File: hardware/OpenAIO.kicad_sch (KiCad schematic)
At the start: 0 parts

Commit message: Root sheet: place the sub-sheets; ESC as the 4in1 top sheet
esc_4in1.kicad_sch is OpenESC-20x20's 4in1-mini top sheet (battery input,
shunt and INA186 current sense, 12V/3V3 regulators, four ESC channel
instances). Its channel sub-sheet keeps its original file name ESC.kicad_sch
so the top sheet is untouched. Root sheet: Power, IMU, OSD, Blackbox, Pads,
RP2354A, ESC, RX placed, no wiring.
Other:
- added sheet Blackbox (fc_blackbox.kicad_sch)
- added sheet ESC (esc_4in1.kicad_sch)
- added sheet IMU (fc_imu.kicad_sch)
- added sheet OSD (fc_osd.kicad_sch)
- added sheet Pads (fc_pads.kicad_sch)
- added sheet Power (fc_power.kicad_sch)
- added sheet RP2354A (fc_rp2350a.kicad_sch)
- added sheet RX (rx_esp32c3_sx1281.kicad_sch)
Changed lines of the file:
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@@
-(kicad_sch
-  (version 20260306)
-  (generator "eeschema")
-  (generator_version "10.0")
-  (paper "A4")
-  (sheet_instances
-    (path "/"
-      (page "1")))
-  (embedded_fonts no))

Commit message: Drop the ESC sheets again; CSA taken into fc_power
esc_4in1 and ESC removed from the root and the tree. fc_power carries
Stan's in-progress edits with the current-sense parts.
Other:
- removed sheet ESC

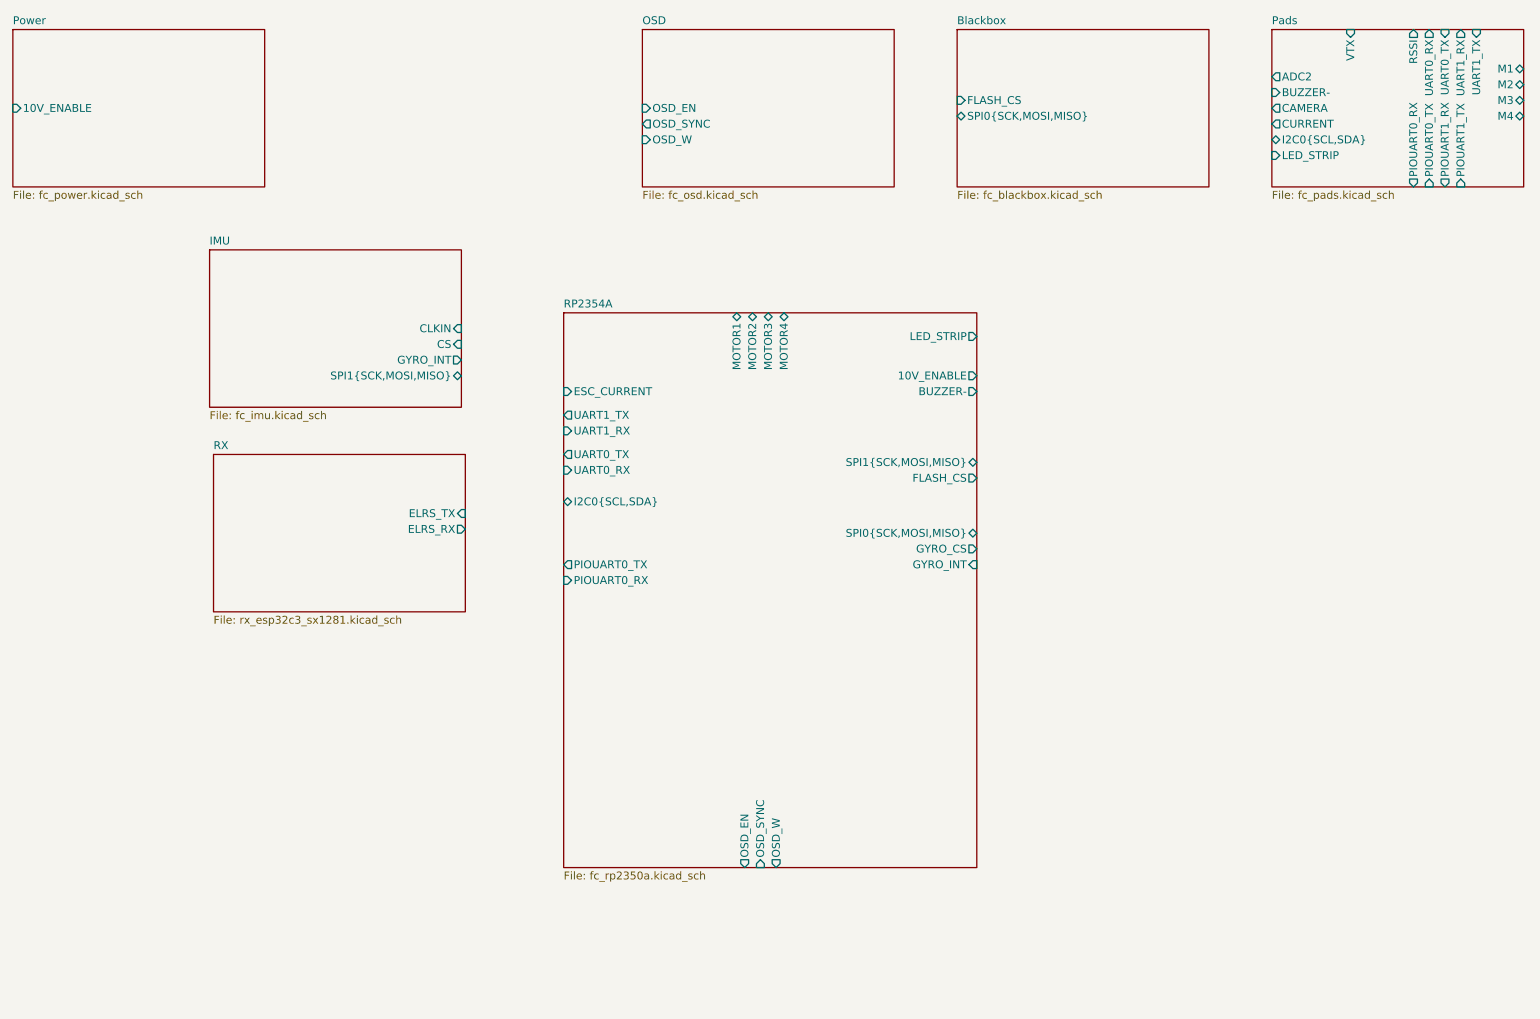
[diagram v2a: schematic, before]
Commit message: Root sheet: ESC1..ESC4 back, one esc_channel instance each
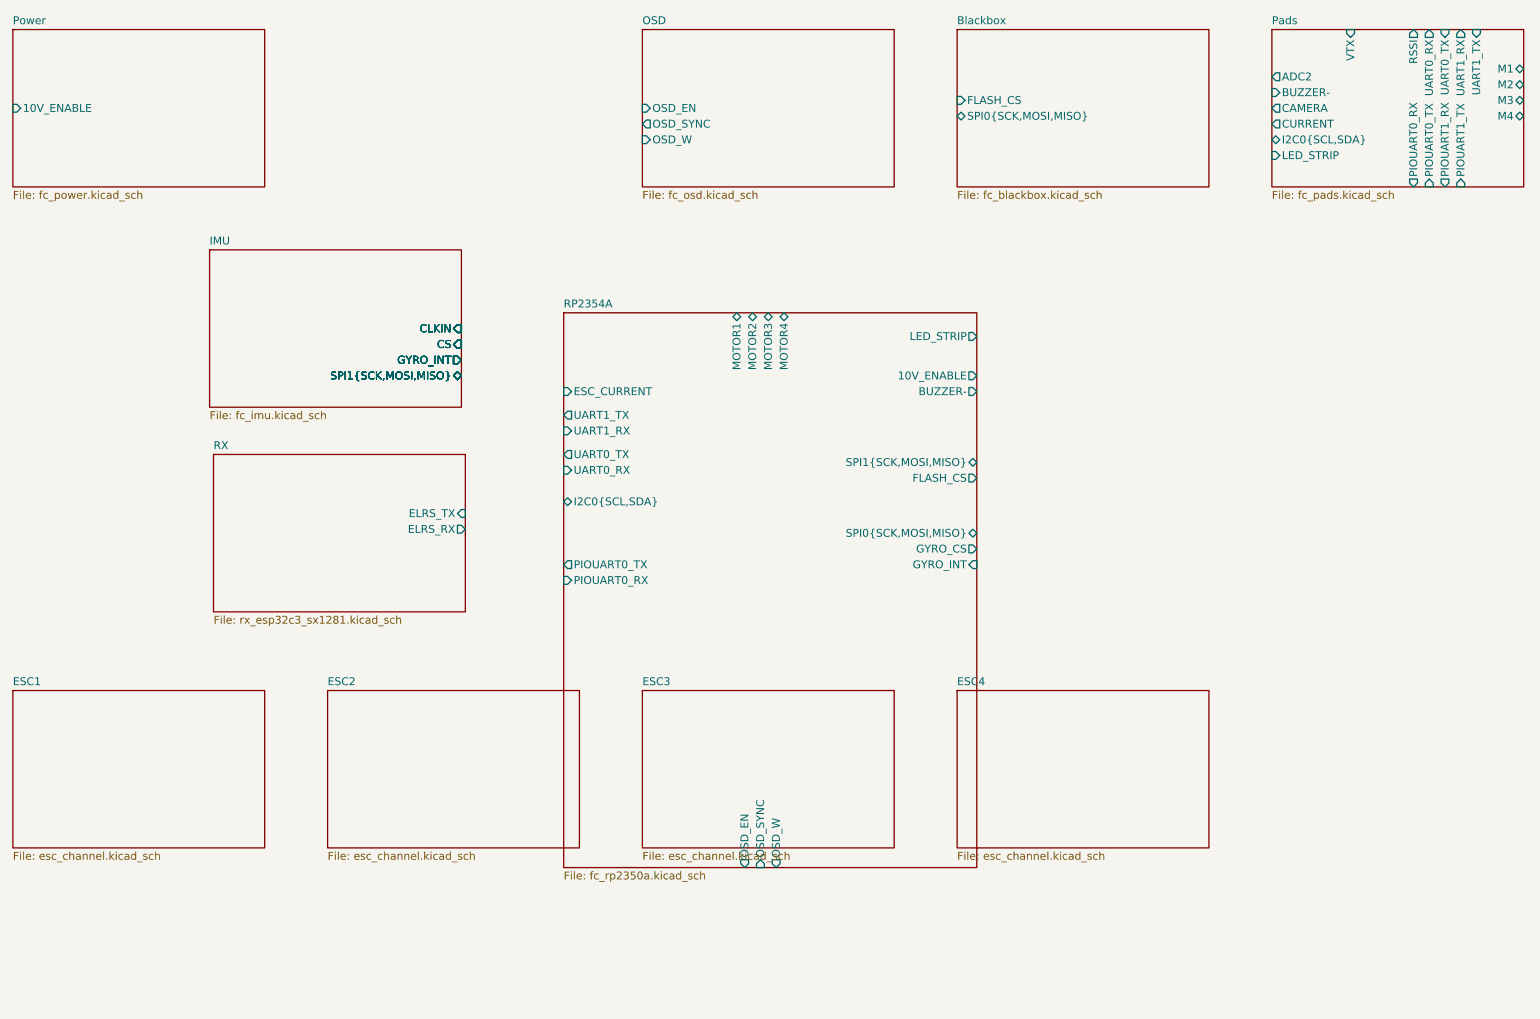
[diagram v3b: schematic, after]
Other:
- added sheet ESC1 (esc_channel.kicad_sch)
- added sheet ESC2 (esc_channel.kicad_sch)
- added sheet ESC3 (esc_channel.kicad_sch)
- added sheet ESC4 (esc_channel.kicad_sch)

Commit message: Restore the root, project and esc_channel to the 21:58 save, before the ESC top sheet
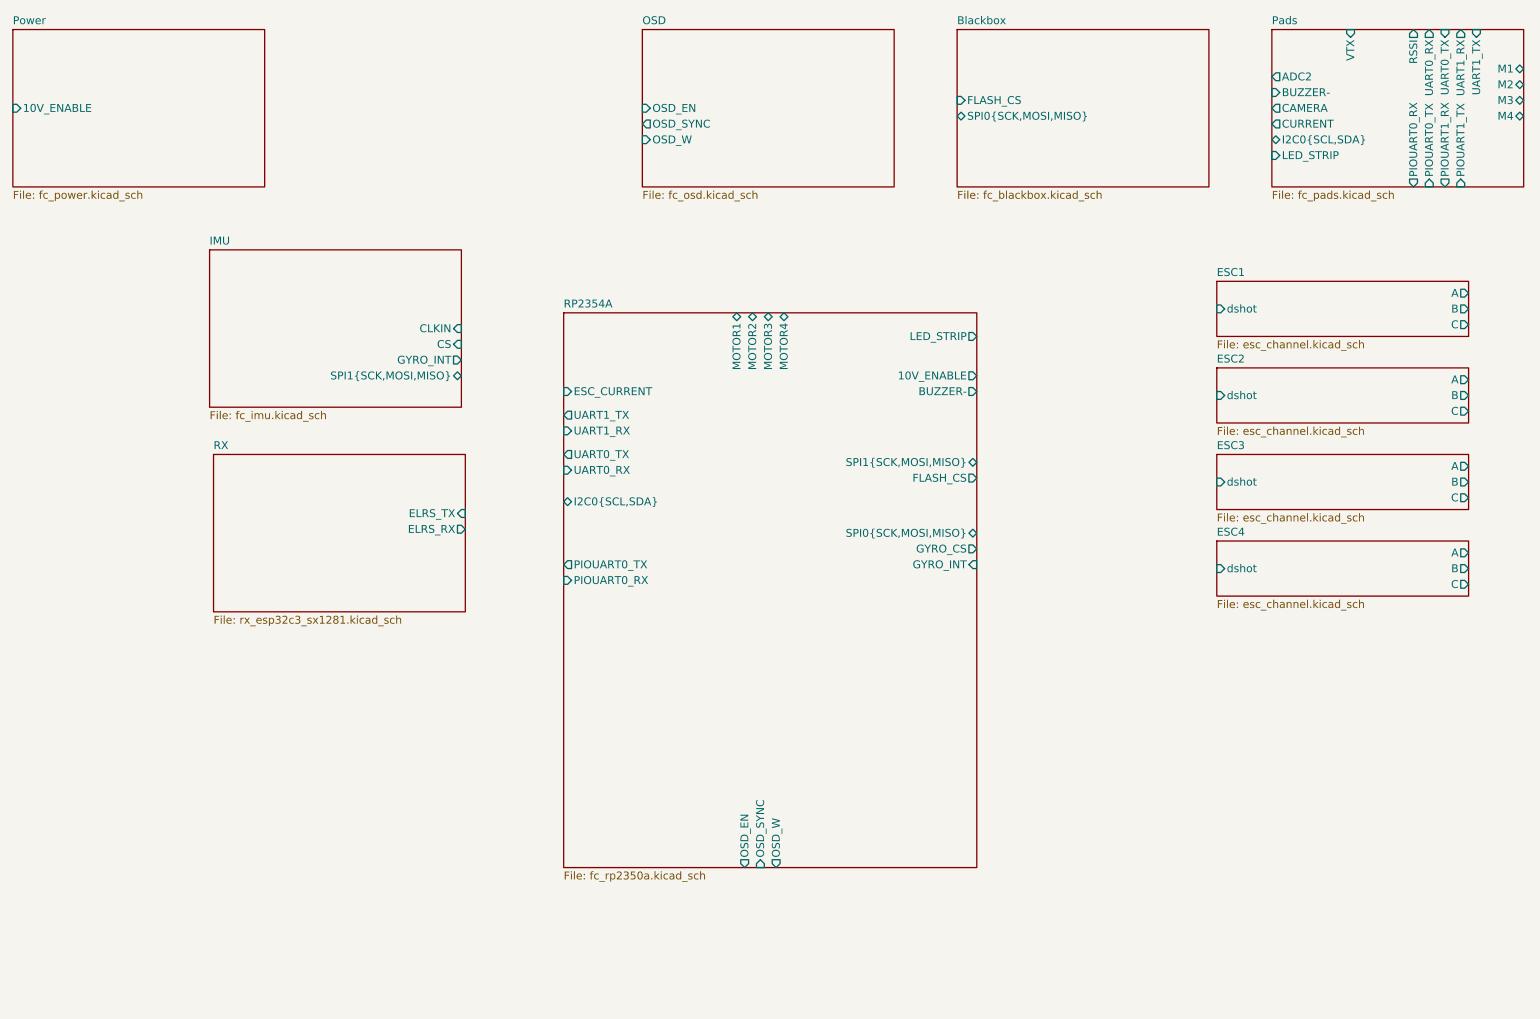
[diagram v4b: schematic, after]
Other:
- sheet ESC1 ports: added A, B, C, dshot; removed CLKIN, CS, GYRO_INT, SPI1{SCK,MOSI,MISO}
- sheet ESC2 ports: added A, B, C, dshot; removed CLKIN, CS, GYRO_INT, SPI1{SCK,MOSI,MISO}
- sheet ESC3 ports: added A, B, C, dshot; removed CLKIN, CS, GYRO_INT, SPI1{SCK,MOSI,MISO}
- sheet ESC4 ports: added A, B, C, dshot; removed CLKIN, CS, GYRO_INT, SPI1{SCK,MOSI,MISO}

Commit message: Net classes: VBAT, Phase, Power, Gate, USB, RF, Analog with colours and patterns
Replaces the stale 50Ohm /ELRS/* patterns inherited from the template.
Widths and clearances start from the line standard (0.09/0.09, via 0.35/0.20)
and the ESC boards' practice; USB and RF geometry still to be checked against
the chosen JLCPCB 6-layer stackup.
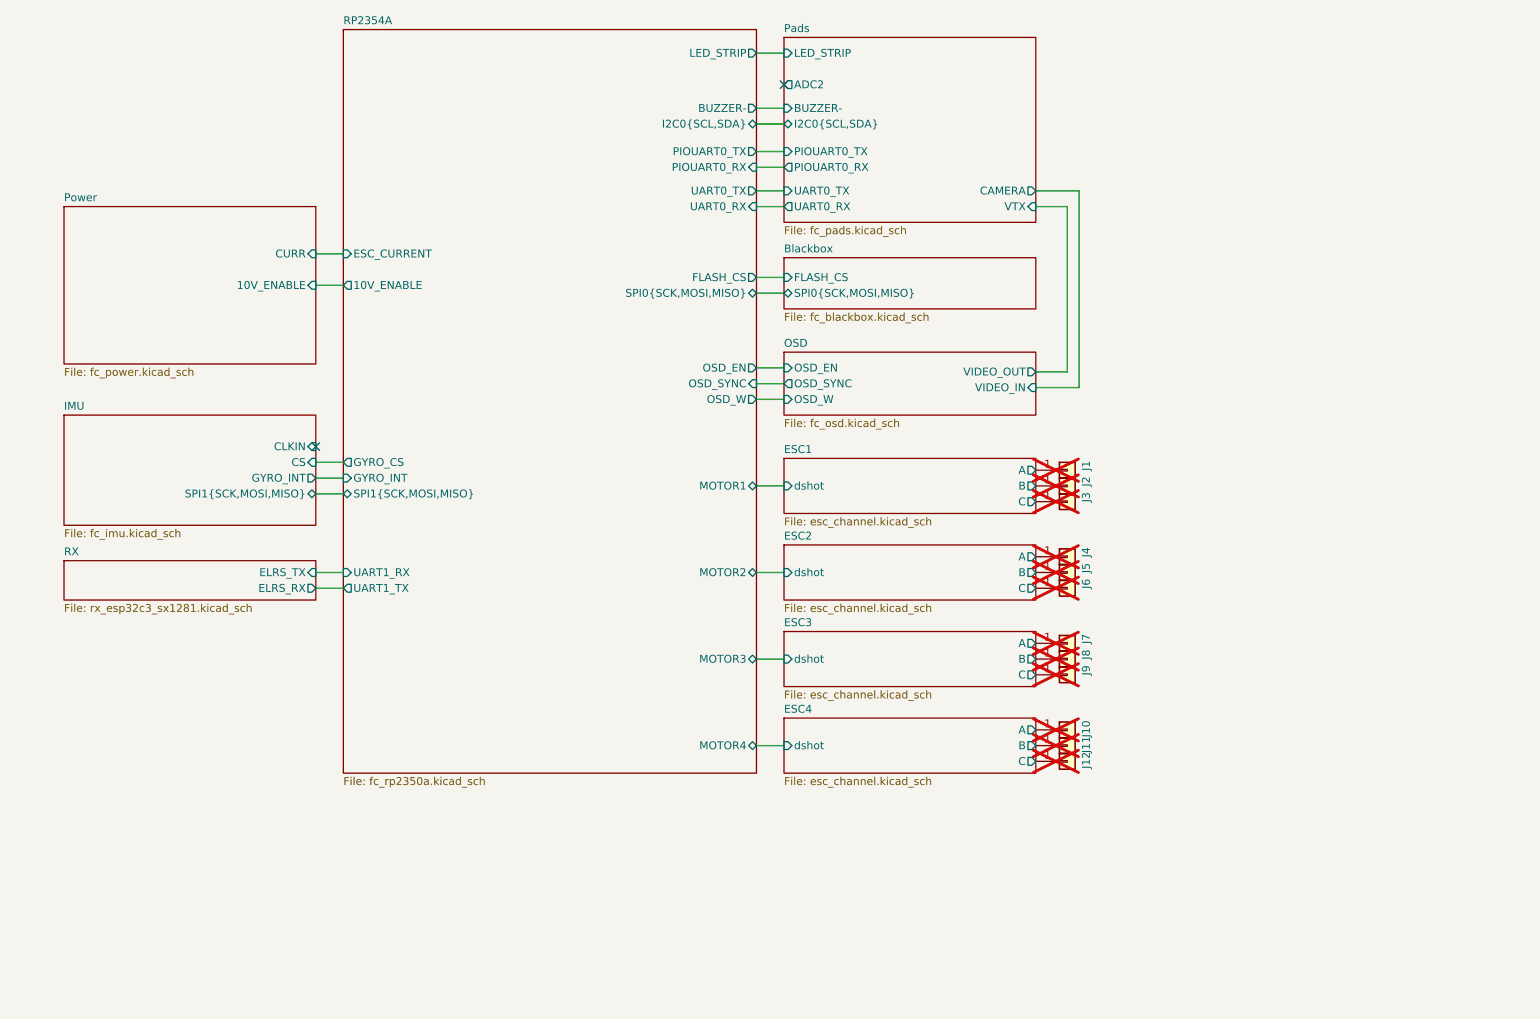
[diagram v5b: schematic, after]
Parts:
- added J1, J10, J11, J12, J2, J3, J4, J5, J6, J7, J8, J9: 5V, lib:small_pad, symbol Connector_Generic:Conn_01x01
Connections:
- net ESC1/A: now also J1.1 (Pin_1)
- net ESC1/B: now also J2.1 (Pin_1)
- net ESC1/C: now also J3.1 (Pin_1)
- net ESC2/A: now also J4.1 (Pin_1)
- net ESC2/B: now also J5.1 (Pin_1)
- net ESC2/C: now also J6.1 (Pin_1)
- net ESC3/A: now also J7.1 (Pin_1)
- net ESC3/B: now also J8.1 (Pin_1)
- net ESC3/C: now also J9.1 (Pin_1)
- net ESC4/A: now also J10.1 (Pin_1)
- net ESC4/B: now also J11.1 (Pin_1)
- net ESC4/C: now also J12.1 (Pin_1)
- no-connect marks 0 -> 2
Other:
- sheet OSD ports: added VIDEO_IN, VIDEO_OUT; removed none
- sheet Pads ports: added none; removed CURRENT, M1, M2, M3, M4, PIOUART1_RX, PIOUART1_TX, RSSI, UART1_RX, UART1_TX
- sheet Power ports: added CURR; removed none

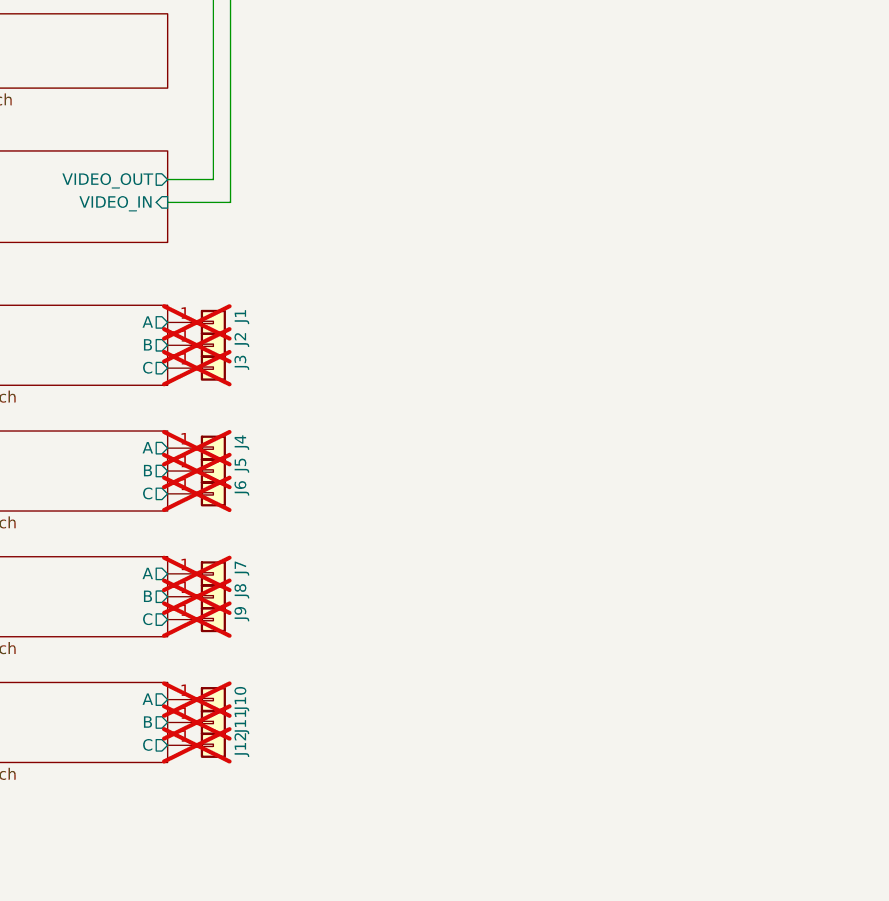
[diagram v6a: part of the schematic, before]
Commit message: OpenAIO: master PCB with Base and Core islands routed, AIO_outline footprint+symbol in project lib
Save point before the two-board (LGA) split tooling.
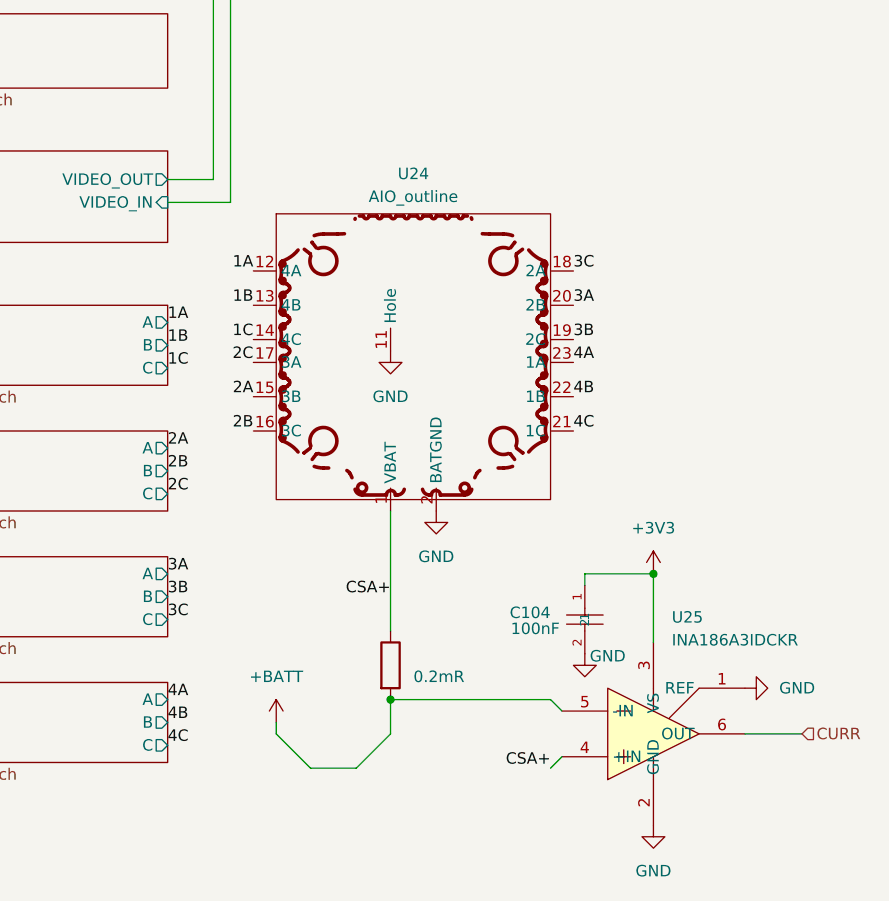
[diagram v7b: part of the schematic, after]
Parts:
- removed J1, J10, J11, J12, J2, J3, J4, J5, J6, J7, J8, J9: 5V, lib:small_pad, symbol Connector_Generic:Conn_01x01
- added C104: 100nF, Capacitor_SMD:C_0201_0603Metric, symbol ESCLibrary:GRM033R61C104KE84D
- added Rsense2: 0.2mR, Resistor_SMD:R_2512_6332Metric, symbol Device:R
- added U24: AIO_outline, OpenDrone:AIO_outline, symbol lib:AIO_outline
- added U25: INA186A3IDCKR, 4in1ESC:SOT-363_SC-70-6, symbol components:INA186A3IDCKR
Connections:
- new net +3V3: C104.1, U25.3 (VS)
- new net +BATT: Rsense2.2, U25.5 (-IN)
- new net 1A: U24.12 (4A)
- new net 1B: U24.13 (4B)
- new net 1C: U24.14 (4C)
- new net 2A: U24.15 (3B)
- new net 2B: U24.16 (3C)
- new net 2C: U24.17 (3A)
- new net 3A: U24.20 (2B)
- new net 3B: U24.19 (2C)
- new net 3C: U24.18 (2A)
- new net 4A: U24.23 (1A)
- new net 4B: U24.22 (1B)
- new net 4C: U24.21 (1C)
- new net CSA+: Rsense2.1, U24.1 (VBAT), U25.4 (+IN)
- new net CURR: U25.6 (OUT)
- new net GND: C104.2, U24.11 (Hole), U24.2 (BATGND), U25.1 (REF), U25.2 (GND)
